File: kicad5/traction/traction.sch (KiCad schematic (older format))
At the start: 0 parts

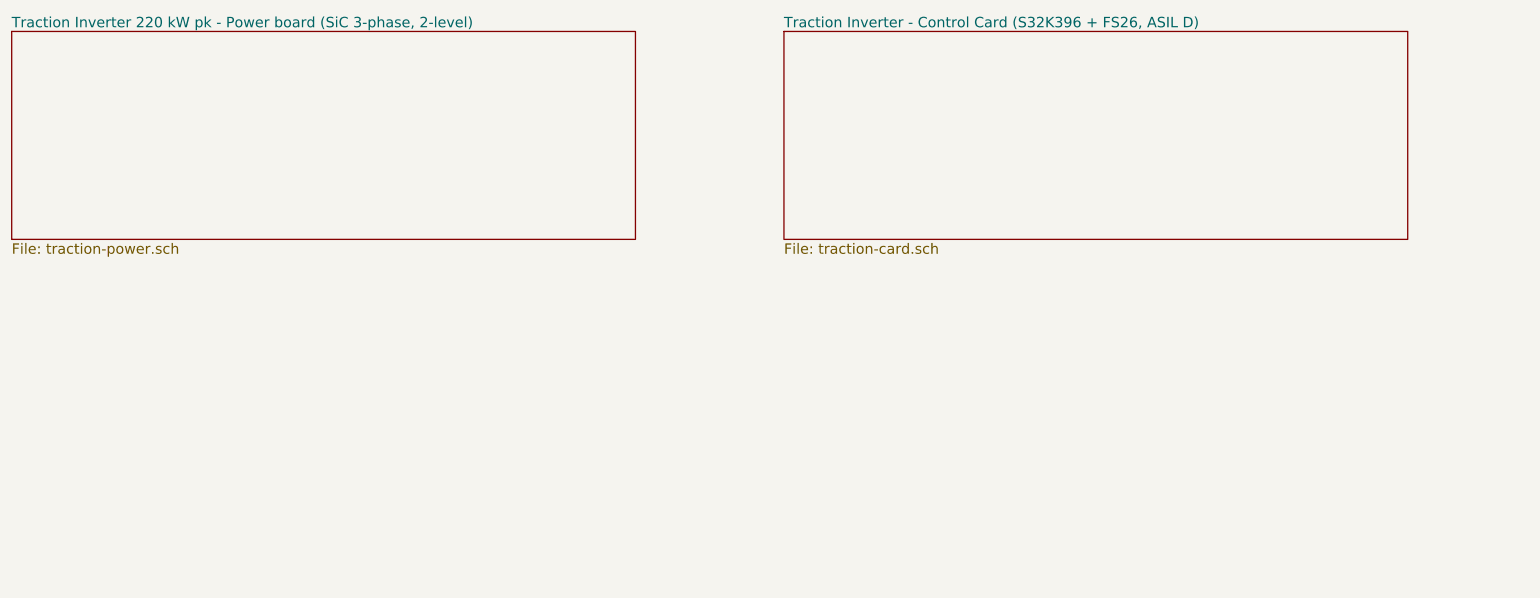
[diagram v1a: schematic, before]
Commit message: Split discharge onto a bolt-on board (XM3 pattern), 3-sheet set
- boards/discharge.tsx: bleeder (2x5x27k) + active discharge (4x470R +
  HCM75S12T4K3, TLP152/QA01C default-OFF) on its own PCB across the cap
  bank; power board keeps JDIS header (V15/QDIS_CMD/2xGND) + CMD pulldown
- pipeline: disch side threaded through pages/gen/verify/print/pdf/bom;
  sheet idents 1..3 of 3; disch title block carries "NEVER energize
  without this board fitted"; root sheet de-branded (X-IN-One -> Traction)
- gates green: 1550/1550 pins, ERC 672/0, design-verify 51P/3W/0F
- docs: README + design-basis + bom synced to 3-board state; new
  docs/img/sheet-disch.png; BOM ₹69,856 @1k (63,375/672/5,808)

Co-Authored-By: Claude Fable 5 <noreply@anthropic.com>
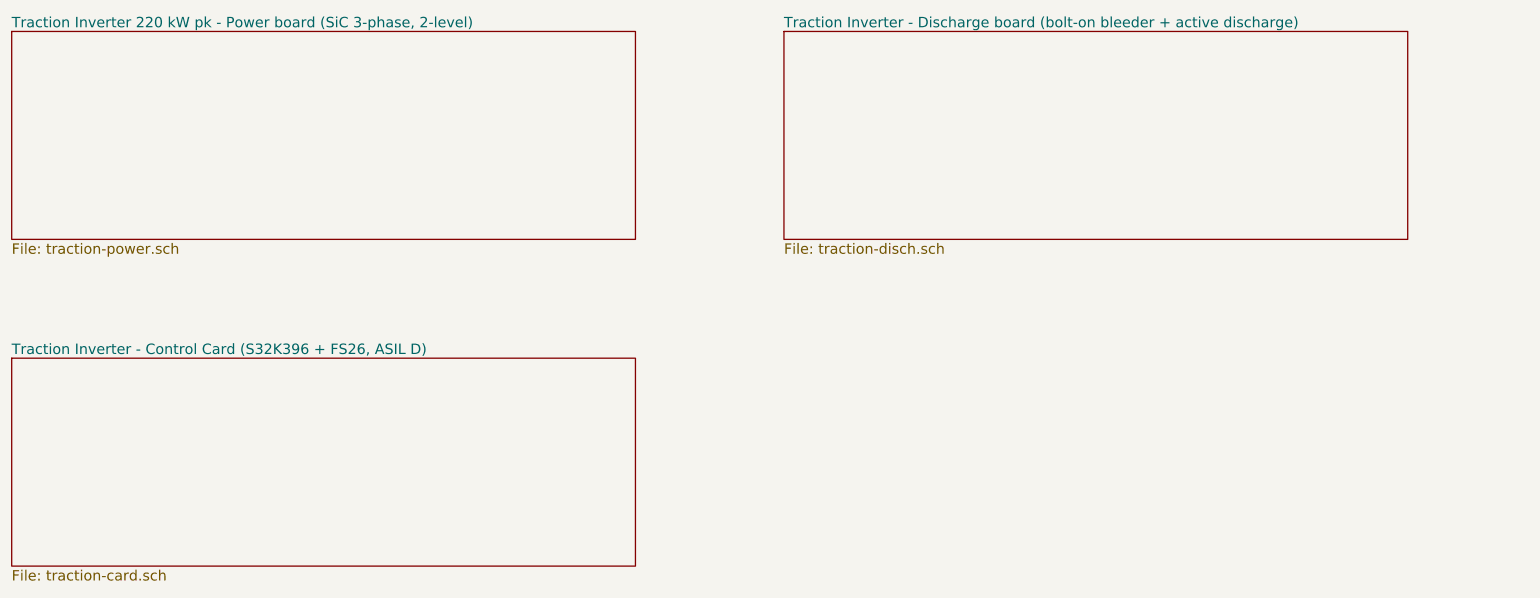
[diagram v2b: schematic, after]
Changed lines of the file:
@@
 Date "2026-09-09"
 Rev "A.3"
-Comp "X-IN-One Traction"
-Comment1 "Power board (SiC 3-phase) sheet 1 - Control card (S32K396+FS26) sheet 2"
+Comp "Traction Inverter"
+Comment1 "Power board (SiC 3-phase) sheet 1 - Discharge board sheet 2 - Control card (S32K396+FS26) sheet 3"
 Comment2 "800 V-class, 120 kW cont / 220 kW pk, ASIL-D-capable architecture"
 Comment3 ""
@@
 $Sheet
 S 1000 1000 4200 1400
-U 5E000212
+U 5E000216
 F0 "Traction Inverter 220 kW pk - Power board (SiC 3-phase, 2-level)" 70
 F1 "traction-power.sch" 70
@@
 $Sheet
 S 6200 1000 4200 1400
-U 5E000213
+U 5E000217
+F0 "Traction Inverter - Discharge board (bolt-on bleeder + active discharge)" 70
+F1 "traction-disch.sch" 70
+$EndSheet
+$Sheet
+S 1000 3200 4200 1400
+U 5E000218
 F0 "Traction Inverter - Control Card (S32K396 + FS26, ASIL D)" 70
 F1 "traction-card.sch" 70

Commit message: Add cap-bank busbar assembly sheet + explicit interboard links (4 sheets)
- boards/capbank.tsx: the 16-can DC-link is its own laminated-busbar
  assembly (FR4 cannot carry the 340 A bus) with every terminal drawn:
  entry lugs, 3x module DC tab pairs, discharge-board studs
- power board keeps only its DCP/DCN entry taps (Y-caps, HVIL, sense)
- interboard links L1-L5 (harness, discharge 4-way, busbar, LEM, HVIL)
  documented in design-basis 10a + README table; erc-audit now asserts
  both ends of every link (new interboard section)
- NET NAMING panels state the cross-sheet net rule on every sheet
- gates green: 1560/1560 pins, ERC 687/0, design-verify 51P/3W/0F
- BOM ₹69,996 @1k (58,575 / 4,940 / 672 / 5,808) · 543 comps · 175 lines

Co-Authored-By: Claude Fable 5 <noreply@anthropic.com>
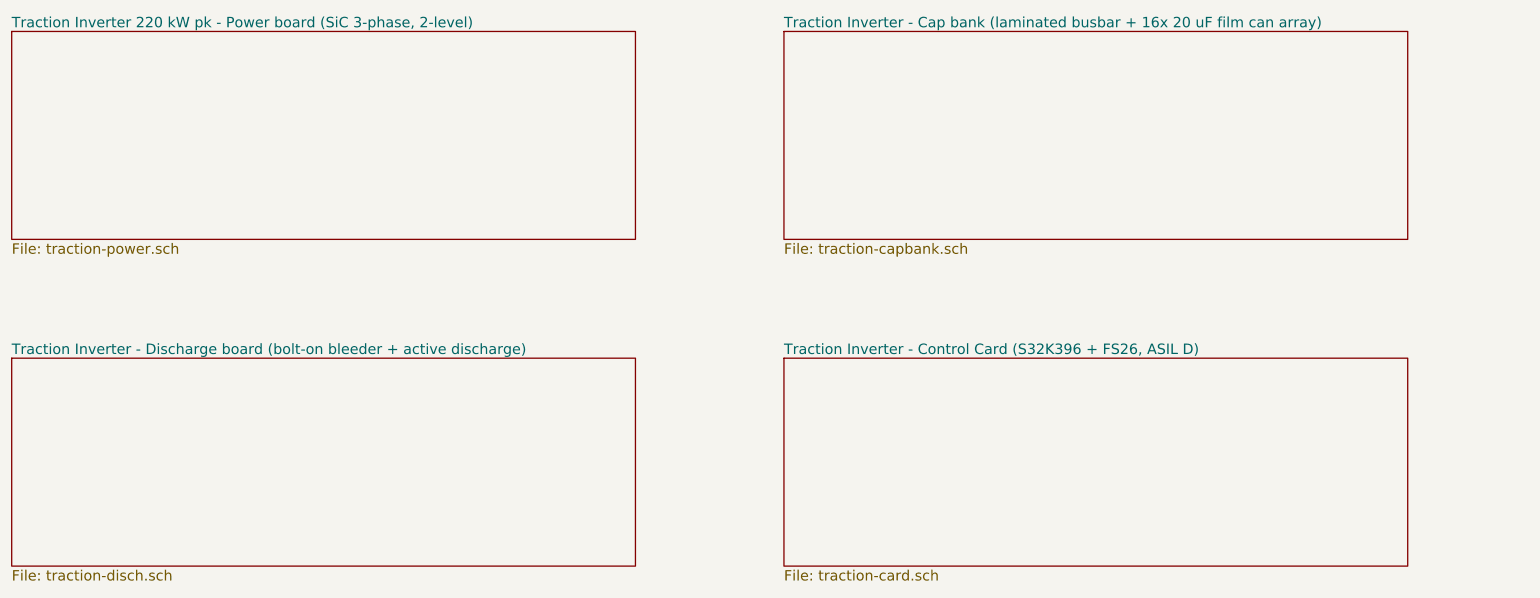
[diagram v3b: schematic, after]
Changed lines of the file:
@@
 Rev "A.3"
 Comp "Traction Inverter"
-Comment1 "Power board (SiC 3-phase) sheet 1 - Discharge board sheet 2 - Control card (S32K396+FS26) sheet 3"
+Comment1 "Power board sheet 1 - Cap bank sheet 2 - Discharge board sheet 3 - Control card sheet 4"
 Comment2 "800 V-class, 120 kW cont / 220 kW pk, ASIL-D-capable architecture"
 Comment3 ""
@@
 $Sheet
 S 1000 1000 4200 1400
-U 5E000216
+U 5E000220
 F0 "Traction Inverter 220 kW pk - Power board (SiC 3-phase, 2-level)" 70
 F1 "traction-power.sch" 70
@@
 $Sheet
 S 6200 1000 4200 1400
-U 5E000217
+U 5E000221
+F0 "Traction Inverter - Cap bank (laminated busbar + 16x 20 uF film can array)" 70
+F1 "traction-capbank.sch" 70
+$EndSheet
+$Sheet
+S 1000 3200 4200 1400
+U 5E000222
 F0 "Traction Inverter - Discharge board (bolt-on bleeder + active discharge)" 70
 F1 "traction-disch.sch" 70
 $EndSheet
 $Sheet
-S 1000 3200 4200 1400
-U 5E000218
+S 6200 3200 4200 1400
+U 5E000223
 F0 "Traction Inverter - Control Card (S32K396 + FS26, ASIL D)" 70
 F1 "traction-card.sch" 70
